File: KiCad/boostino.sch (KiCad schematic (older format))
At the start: 9 parts, among them J1 Conn_01x14_Female, J2 Conn_01x04_Male, Q1 2N3904, U1 Teensy3.6

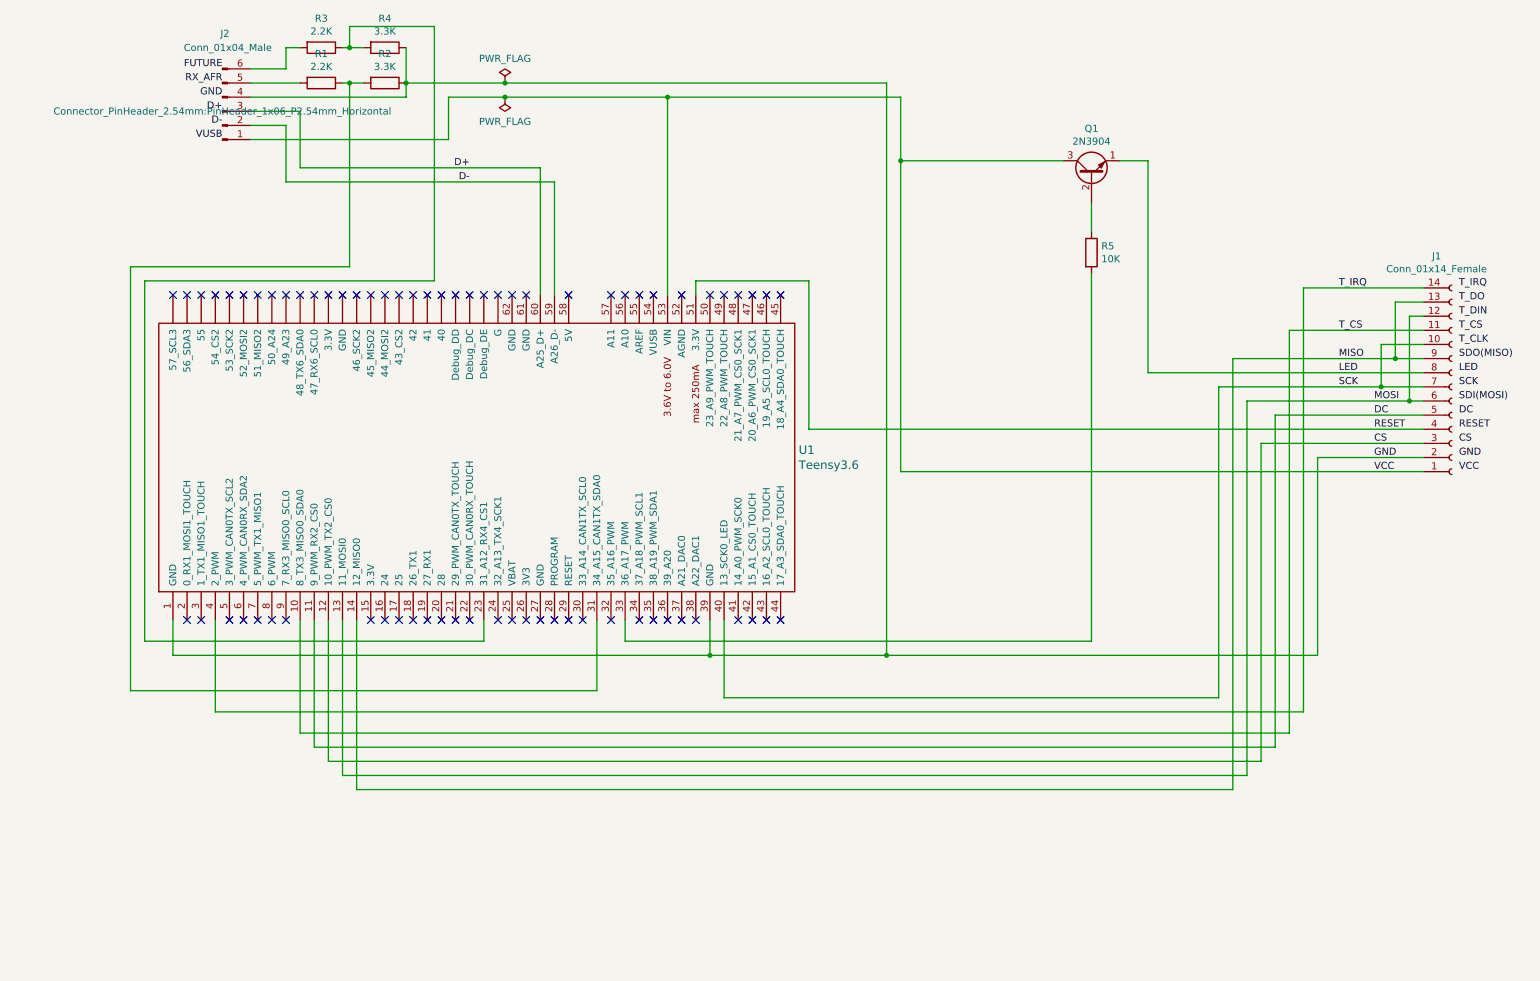
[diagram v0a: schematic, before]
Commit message: Updated PCB for MC33660. Still need to regenerate Gerber files.
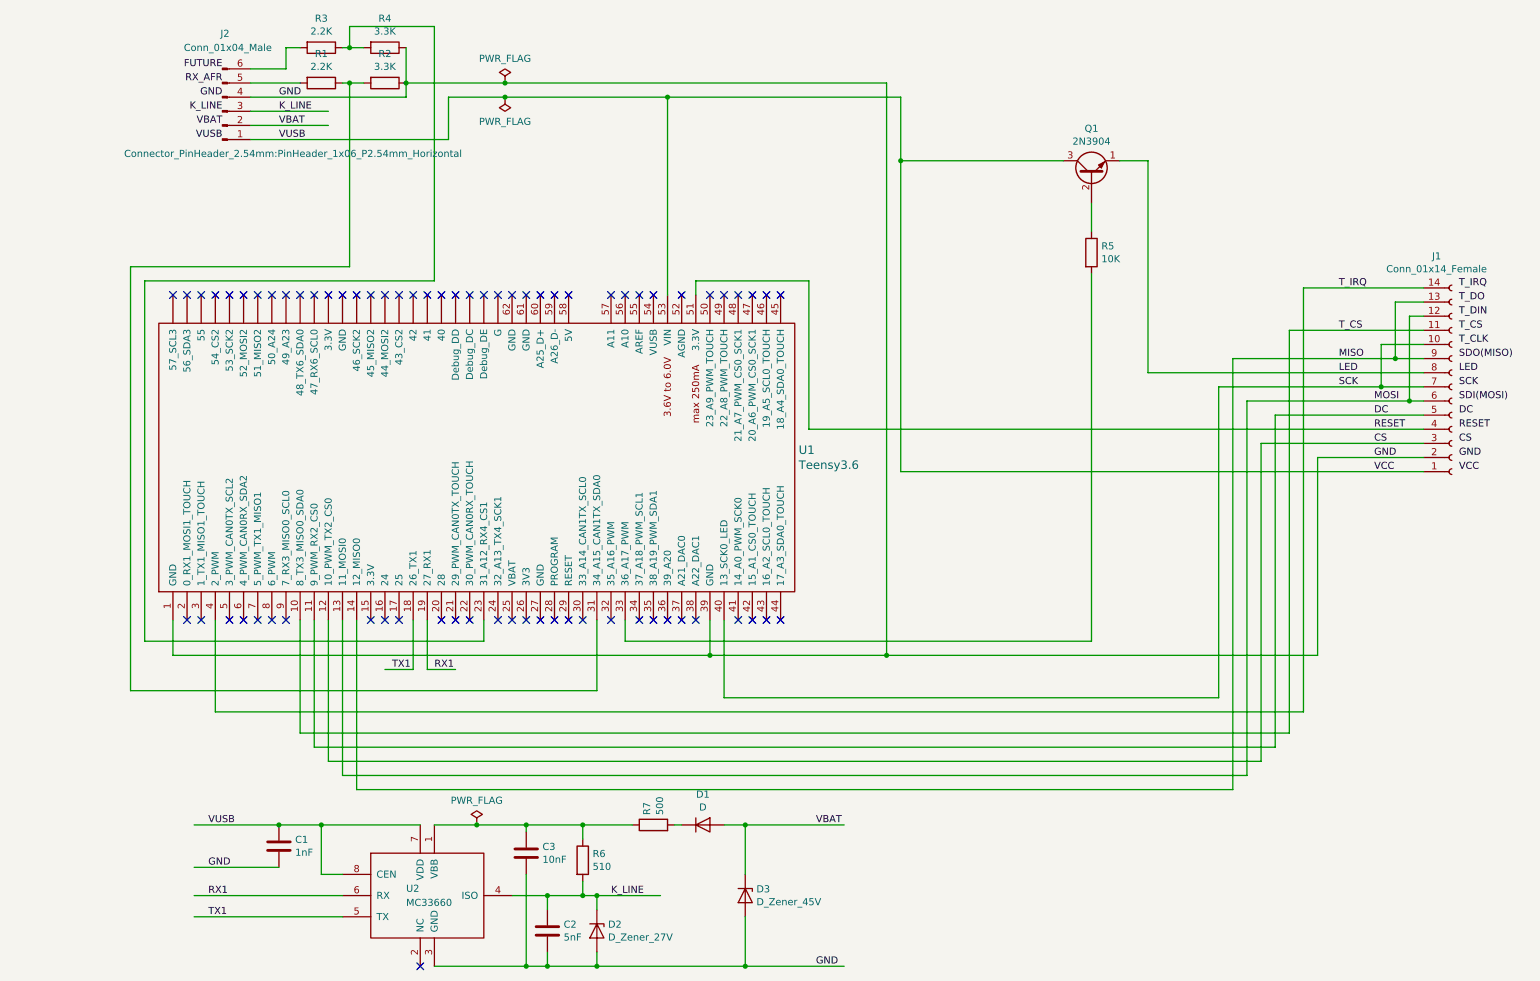
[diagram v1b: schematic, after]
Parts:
- added C1: 1nF, Capacitor_SMD:C_1206_3216Metric_Pad1.42x1.75mm_HandSolder, symbol Device:C
- added C2: 5nF, Capacitor_SMD:C_1206_3216Metric_Pad1.42x1.75mm_HandSolder, symbol Device:C
- added C3: 10nF, Capacitor_SMD:C_1206_3216Metric_Pad1.42x1.75mm_HandSolder, symbol Device:C
- added D1: D, Diode_THT:D_A-405_P10.16mm_Horizontal, symbol Device:D
- added D2: D_Zener_27V, Diode_SMD:D_MiniMELF_Handsoldering, symbol Device:D_Zener
- added D3: D_Zener_45V, Diode_SMD:D_MiniMELF_Handsoldering, symbol Device:D_Zener
- added R6: 510, Resistor_SMD:R_0805_2012Metric_Pad1.15x1.40mm_HandSolder, symbol Device:R
- added R7: 500, Resistor_SMD:R_0805_2012Metric_Pad1.15x1.40mm_HandSolder, symbol Device:R
- added U2: MC33660, Package_SO:SOIC-8_3.9x4.9mm_P1.27mm, symbol MC33660:MC33660
- R1, R2, R3, R4, R5: footprint Resistor_THT:R_Axial_DIN0207_L6.3mm_D2.5mm_P10.16mm_Horizontal -> Resistor_SMD:R_0805_2012Metric_Pad1.15x1.40mm_HandSolder
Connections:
- net labels added: K_LINE, RX1, TX1, VBAT
- net labels removed: D+, D-
- wire segments 99 -> 131
- no-connect marks 70 -> 71

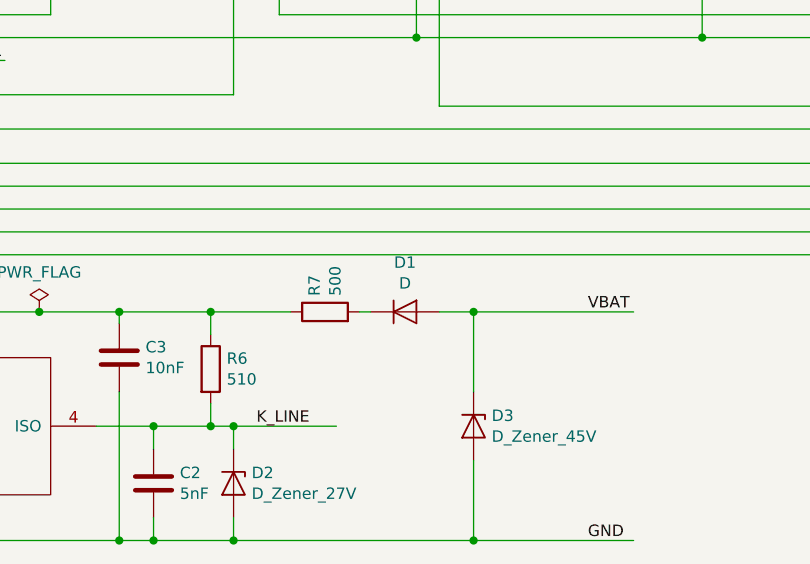
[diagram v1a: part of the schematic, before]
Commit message: Label diode in schematic
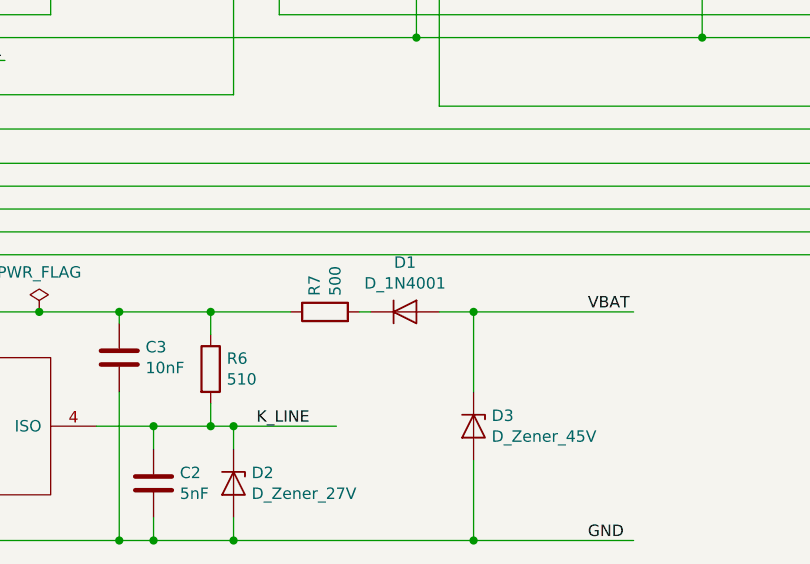
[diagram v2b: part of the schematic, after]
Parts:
- D1: value D -> D_1N4001
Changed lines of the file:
@@
 P 4700 6550
 F 0 "D1" H 4700 6766 50  0000 C CNN
-F 1 "D" H 4700 6675 50  0000 C CNN
+F 1 "D_1N4001" H 4700 6675 50  0000 C CNN
 F 2 "Diode_THT:D_A-405_P10.16mm_Horizontal" H 4700 6550 50  0001 C CNN
 F 3 "~" H 4700 6550 50  0001 C CNN

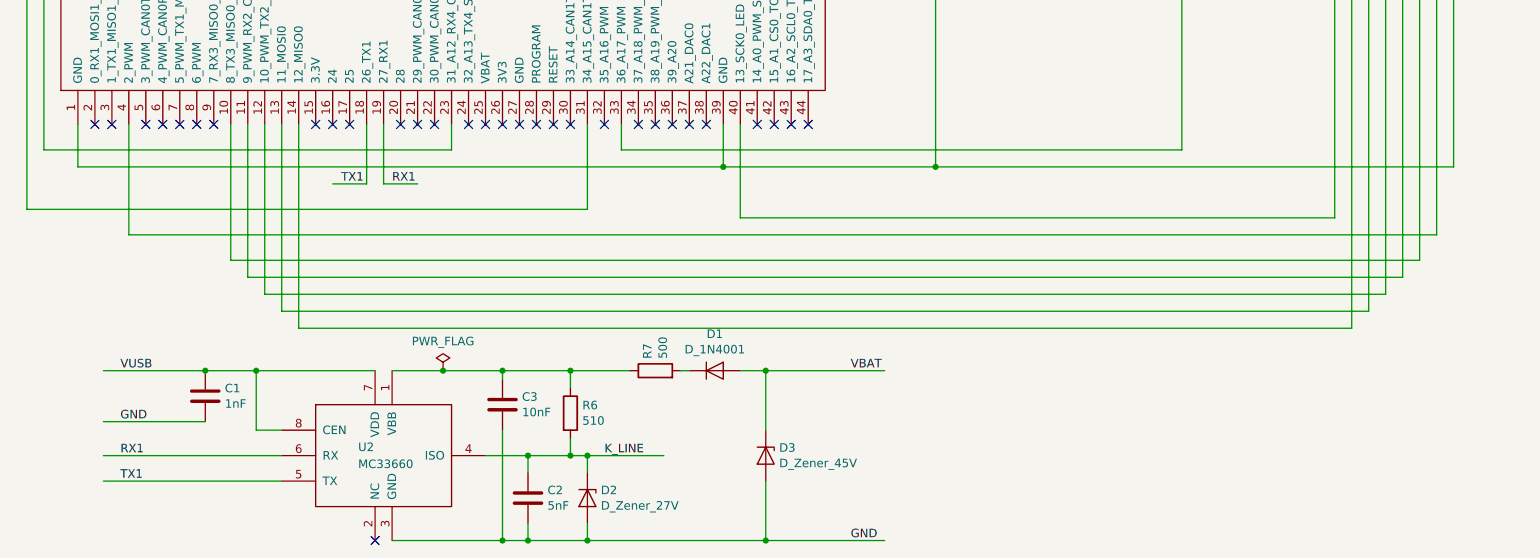
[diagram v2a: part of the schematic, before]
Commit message: Update PCB to use Serial3 for K-Line
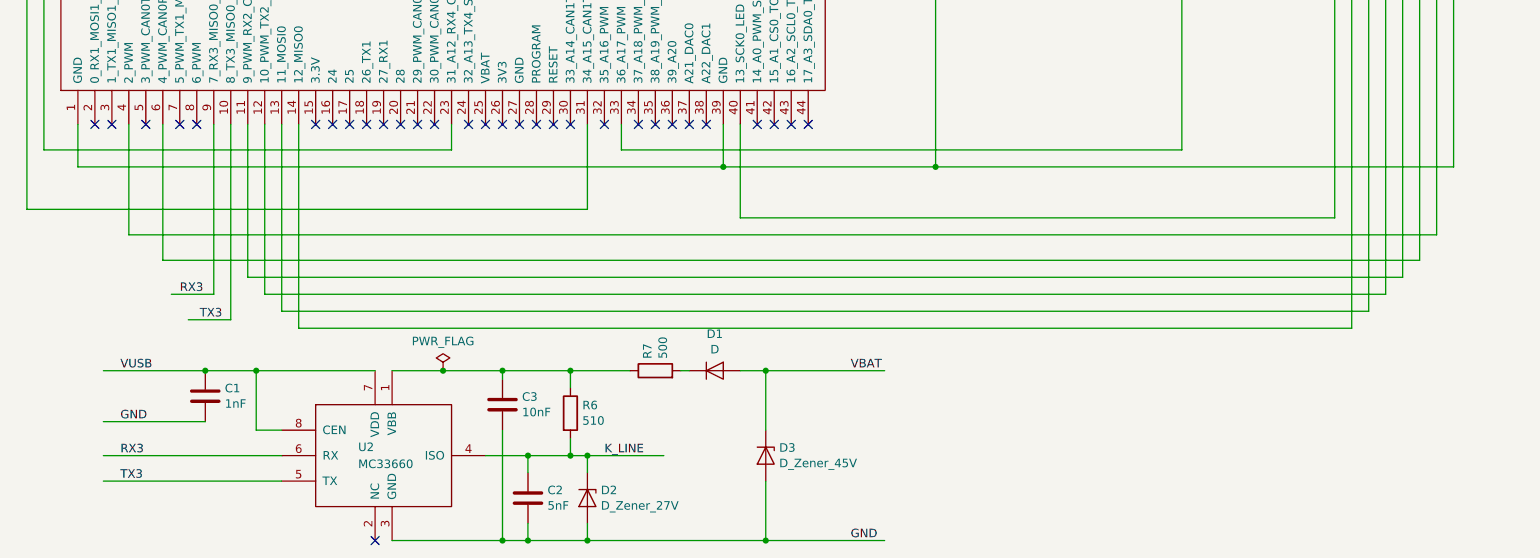
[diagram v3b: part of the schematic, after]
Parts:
- D1: value D_1N4001 -> D
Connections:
- net labels added: RX3, TX3
- net labels removed: RX1, TX1
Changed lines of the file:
@@
 	8950 2750 9800 2750
 Wire Wire Line
-	1850 5100 1850 5900
-Wire Wire Line
-	1850 5900 8850 5900
+	1450 5100 1450 5900
+Wire Wire Line
+	1450 5900 8850 5900
 Wire Wire Line
 	8850 5900 8850 3050
@@
 NoConn ~ 1150 5100
 NoConn ~ 1350 5100
-NoConn ~ 1450 5100
 NoConn ~ 1550 5100
-NoConn ~ 1650 5100
-NoConn ~ 1750 5100
 NoConn ~ 2450 5100
 NoConn ~ 2550 5100
@@
 Wire Wire Line
 	3300 1300 6000 1300
-$Comp
-L teensy:Teensy3.6 U1
-U 1 1 5E36506E
-P 3100 3950
-F 0 "U1" V 3153 1672 60  0000 R CNN
-F 1 "Teensy3.6" V 3047 1672 60  0000 R CNN
-F 2 "Teensy:Teensy35_36" H 3100 4000 60  0001 C CNN
-F 3 "" H 3100 4000 60  0000 C CNN
-	1    3100 3950
-	0    -1   -1   0
-$EndComp
 Wire Wire Line
 	4650 2800 4650 2700
@@
 	3850 7050 3950 7050
 $Comp
-L Device:D D1
-U 1 1 5F78823F
-P 4700 6550
-F 0 "D1" H 4700 6766 50  0000 C CNN
-F 1 "D_1N4001" H 4700 6675 50  0000 C CNN
-F 2 "Diode_THT:D_A-405_P10.16mm_Horizontal" H 4700 6550 50  0001 C CNN
-F 3 "~" H 4700 6550 50  0001 C CNN
-	1    4700 6550
-	1    0    0    -1
-$EndComp
-$Comp
 L Device:R R7
 U 1 1 5F78930C
@@
 	5000 6550 5000 6900
 Wire Wire Line
-	2750 5100 2750 5450
-Wire Wire Line
-	2750 5450 2950 5450
-Wire Wire Line
-	2650 5100 2650 5450
-Wire Wire Line
-	2650 5450 2450 5450
-Text Label 2800 5450 0    50   ~ 0
-RX1
-Text Label 2500 5450 0    50   ~ 0
-TX1
+	1850 5100 1850 6250
+Wire Wire Line
+	1850 6250 1600 6250
+Text Label 1800 6250 2    50   ~ 0
+TX3
 Wire Wire Line
 	1100 7050 2150 7050
@@
 	2150 7200 1100 7200
 Text Label 1200 7050 0    50   ~ 0
-RX1
+RX3
 Text Label 1200 7200 0    50   ~ 0
-TX1
+TX3
 NoConn ~ 2700 7550
 $Comp
@@
 Wire Wire Line
 	1700 6550 2000 6550
+NoConn ~ 1650 5100
+$Comp
+L Device:D D1
+U 1 1 5F78823F
+P 4700 6550
+F 0 "D1" H 4700 6766 50  0000 C CNN
+F 1 "D" H 4700 6675 50  0000 C CNN
+F 2 "Diode_THT:D_A-405_P10.16mm_Horizontal" H 4700 6550 50  0001 C CNN
+F 3 "~" H 4700 6550 50  0001 C CNN
+	1    4700 6550
+	1    0    0    -1
+$EndComp
+Text Label 1550 6100 0    50   ~ 0
+RX3
+Wire Wire Line
+	1750 5100 1750 6100
+Wire Wire Line
+	1750 6100 1500 6100
+$Comp
+L teensy:Teensy3.6 U1
+U 1 1 5E36506E
+P 3100 3950
+F 0 "U1" V 3153 1672 60  0000 R CNN
+F 1 "Teensy3.6" V 3047 1672 60  0000 R CNN
+F 2 "Teensy:Teensy35_36" H 3100 4000 60  0001 C CNN
+F 3 "" H 3100 4000 60  0000 C CNN
+	1    3100 3950
+	0    -1   -1   0
+$EndComp
+NoConn ~ 2650 5100
+NoConn ~ 2750 5100
 $EndSCHEMATC
